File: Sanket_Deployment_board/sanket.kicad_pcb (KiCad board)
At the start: 2 copper layers, 92 x 95.9 mm, 38 parts, among them J1 Conn_01x03, J2 Conn_02x03_Counter_Clockwise, J3 Conn_02x03_Counter_Clockwise, J4 Conn_01x01_Socket, J7 Conn_01x01_Socket, J8 Conn_01x05, Q1 NMOS, Q2 NMOS, U2 SN74LVC1G17QDCKRQ1, U3 TPS5420D, U4 74AHC1G00

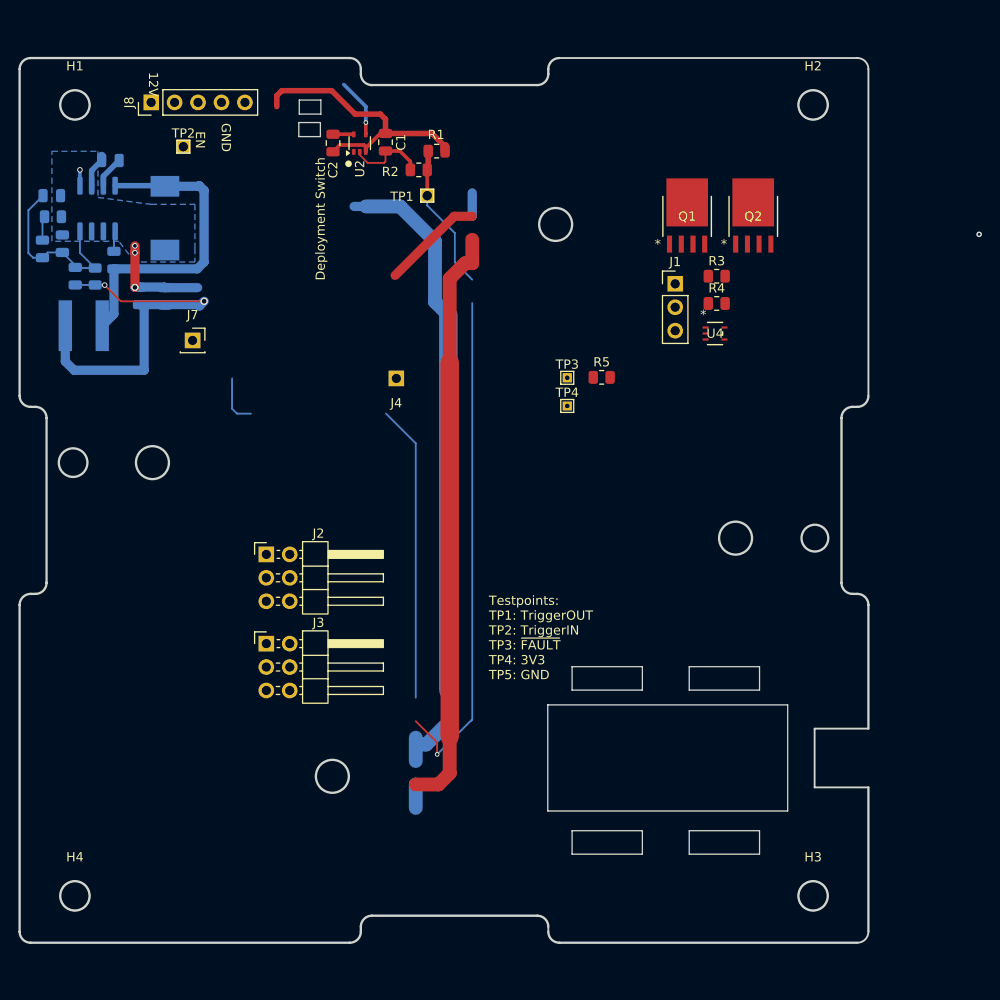
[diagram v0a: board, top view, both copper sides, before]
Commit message: Switch footprint flipped to opposite side, Edgecut layer updated according to new resistor board
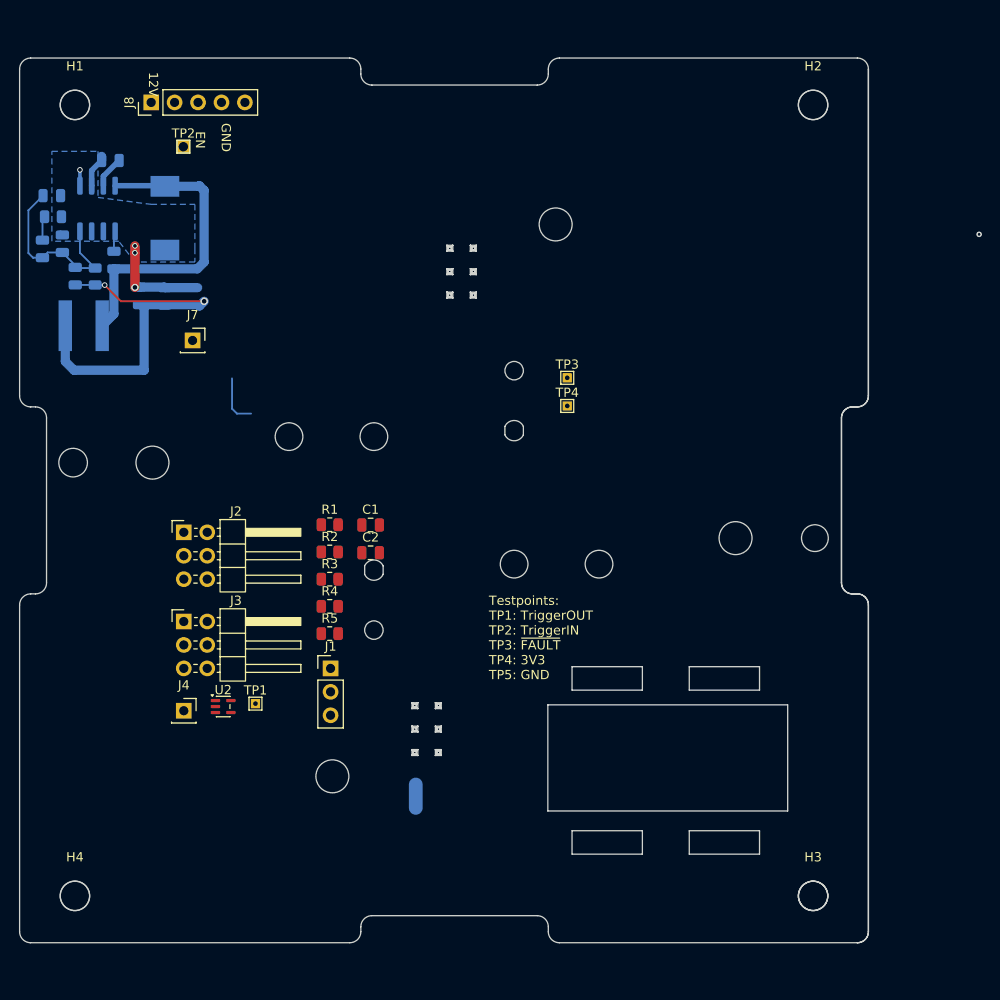
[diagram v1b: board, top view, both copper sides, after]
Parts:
- removed Q1, Q2: NMOS, NMOS_sanket:LFPAK56_SOT669_NEX-M
- removed U4: 74AHC1G00, NAND_sanket:DCK5_TEX-L
- C1: value 2u2 -> ~
- C10: value 4.7u -> ~
- C2, C8: value 100n -> ~
- C3: value 10n -> ~
- C4, C5: value 47u -> ~
- C6: value 150p -> ~
- C9: value 1800p -> ~
- D1: value D -> ~
- H1, H2, H3, H4: value MountingHole -> ~
- J1: value Conn_01x03 -> ~
- J4: value Conn_01x01_Socket -> ~; moved to F.Cu
- J7: value Conn_01x01_Socket -> ~
- J8: value Conn_01x05 -> ~
- L1: value 18u -> ~
- R1: value 1k -> ~
- R2, R3, R4: value 100k -> ~
- R5: value 1M -> ~
- R6: value 549 -> ~
- R7: value 5.9K -> ~
- R8: value 10k -> ~
- TP1, TP2, TP3, TP4: value TestPoint -> ~
- U2: value SN74LVC1G17QDCKRQ1 -> ~
- U3: value TPS5420D -> ~
- moved U2 62.8 mm to (118.4, 119.6), turned to 0 degrees
- moved TP1 58.1 mm to (121.9, 119.3)
- moved J1 56.0 mm to (130.0, 115.4)
- moved R3 53.3 mm to (129.9, 105.8)
- moved R4 53.3 mm to (129.9, 108.7)
- moved C2 44.6 mm to (134.3, 102.9), turned to 0 degrees
- moved J4 42.8 mm to (114.1, 120.0), turned to 0 degrees
- moved R2 42.5 mm to (129.9, 102.8), turned to 0 degrees
- moved R1 42.1 mm to (129.9, 99.9)
- moved C1 41.5 mm to (134.3, 99.9), turned to 0 degrees
- moved R5 40.5 mm to (129.9, 111.7)
- moved J2 9.26 mm to (114.1, 100.7)
- moved J3 9.26 mm to (114.1, 110.4)
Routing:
- net (no net): track 121.1 -> 2.54 mm, vias 2 -> 1
- net /BurnWire1IN: track 70.1 -> 0.00 mm
- net GND: track 60.7 -> 15.9 mm
- net /3V3: track 82.5 -> 48.2 mm
- net /DeployerDetectionSW2OUT: track 16.2 -> 0.00 mm
- net /TriggerIN: track 8.75 -> 0.00 mm
- net /TriggerOUT: track 6.39 -> 0.00 mm, vias 1 -> 0
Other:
- outline, holes or cut-outs redrawn
- board text removed: "Current Sensor"
- board text removed: "Deployment Switch"
- board text removed: "J4"
- board text removed: "TP1"
- board text removed: "TP5"

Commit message: Routing done, 1st review to be done
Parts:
- removed J7: ~, Connector_PinSocket_2.54mm:PinSocket_1x01_P2.54mm_Vertical
- removed TP3, TP4: ~, TestPoint:TestPoint_THTPad_1.0x1.0mm_Drill0.5mm
- added NMOS1: BUK9Y21-40E_115, NMOS_sanket:LFPAK56_SOT669_NEX-M, B.Cu at (116.6, 114.8)
- added NMOS2: BUK9Y21-40E_115, NMOS_sanket:LFPAK56_SOT669_NEX-M, B.Cu at (116.0, 124.1)
- added U1: SN74LV1T00DCKR, NAND_sanket:DCK5_TEX-L, B.Cu at (124.5, 128.3)
- C1, C2, J1, J4, J8, R1, R2, R3, R4, R5, TP1, TP2: moved to B.Cu
- D1: footprint Wurth inductor:DIOM7959X261N -> Diode_in_TP5420:CR_MBRS340_ONS-M
- U2: footprint Package_TO_SOT_SMD:SOT-353_SC-70-5 -> Schmitt_trigger_ADS:DCK5-M; moved to B.Cu
- U3: footprint Package_SO:SOIC-8_3.9x4.9mm_P1.27mm -> TPS5420:D8-M
- moved H4 89.1 mm to (191.3, 143.3), turned to 90 degrees
- moved H1 89.0 mm to (105.6, 143.3), turned to 90 degrees
- moved C6 82.6 mm to (114.7, 145.4), turned to -90 degrees
- moved J8 81.1 mm to (105.3, 135.0), turned to 0 degrees
- moved R6 80.6 mm to (117.0, 145.3), turned to 90 degrees
- moved C8 79.1 mm to (119.8, 146.2), turned to 0 degrees
- moved C10 78.9 mm to (110.2, 139.1), turned to -90 degrees
- moved H3 77.3 mm to (191.3, 63.3), turned to 90 degrees
- moved H2 77.3 mm to (105.6, 63.3), turned to 90 degrees
- moved R7 77.0 mm to (119.8, 144.1), turned to 180 degrees
- moved U3 75.1 mm to (116.0, 139.9), turned to 180 degrees
- moved C9 72.5 mm to (123.4, 142.3), turned to 180 degrees
- moved R8 69.8 mm to (123.4, 140.1), turned to 180 degrees
- moved L1 69.5 mm to (129.8, 142.5), turned to -90 degrees
- moved C3 68.7 mm to (122.5, 138.0), turned to 180 degrees
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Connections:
- J2 pad 1: /3V3 -> /BurnWire1IN
- J2 pad 2: /DeployerDetectionSW1OUT -> /BurnWire1OUT
- J2 pad 4: /BurnWire1IN -> /BurnWire1OUT
- J2 pad 5: /BurnWire1OUT -> /DeployerDetectionSW1OUT
- J2 pad 6: /BurnWire1OUT -> /3V3
- J3 pad 1: /DeployerDetectionSW1OUT -> /BurnWire1OUT
- J3 pad 2: /DeployerDetectionSW2OUT -> /NMOS_DRAIN
- J3 pad 4: /BurnWire1OUT -> /NMOS_DRAIN
- J3 pad 5: GND -> /DeployerDetectionSW2OUT
- J3 pad 6: GND -> /DeployerDetectionSW1OUT
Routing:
- net /BurnWire1IN: track 0.00 -> 85.7 mm
- net /BurnWire1OUT: track 0.00 -> 67.4 mm
- net /3V3: track 48.2 -> 103.5 mm, vias 2 -> 4
- net /DeployerDetectionSW1OUT: track 0.00 -> 46.1 mm
- net /12V: track 3.44 -> 37.6 mm
- net /FIRE: track 0.00 -> 33.5 mm, vias 0 -> 1
- net /DeployerDetectionSW2OUT: track 0.00 -> 20.8 mm
- net /ARM: track 0.00 -> 20.6 mm, vias 0 -> 1
- net Net-(MOSFET1-Pad1): track 0.00 -> 20.1 mm
- net /DEPLOY: track 0.00 -> 19.6 mm
- net /NMOS_DRAIN: track 0.00 -> 18.8 mm
- net /TriggerOUT: track 0.00 -> 7.40 mm
- net /TriggerIN: track 0.00 -> 5.13 mm
- net GND: track 15.9 -> 10.9 mm, vias 3 -> 0
- net Net-(D1-K): track 34.6 -> 30.9 mm, vias 0 -> 2
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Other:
- board size 92 x 95.9 mm -> 95.9 x 92 mm
- board text added: "3V3"
- board text added: "ARM"
- board text added: "BURN1_OUT"
- board text added: "BURNIN"
- board text added: "DEPLOY"
- board text added: "DEPLOYER1_OUT"
- board text added: "FIRE"
- board text removed: "${REFERENCE}"
- board text removed: "Antenna Deployment Board 7 Manyaman Naik, ${COMPANY} 2026-01-09"
- board text removed: "EN"
- board text removed: "TP2"
- board text removed: "TP4"
- board text removed: "Testpoints: TP1: TriggerOUT TP2: TriggerIN TP3: ~{FAULT} TP4: 3V3 TP5: GND"

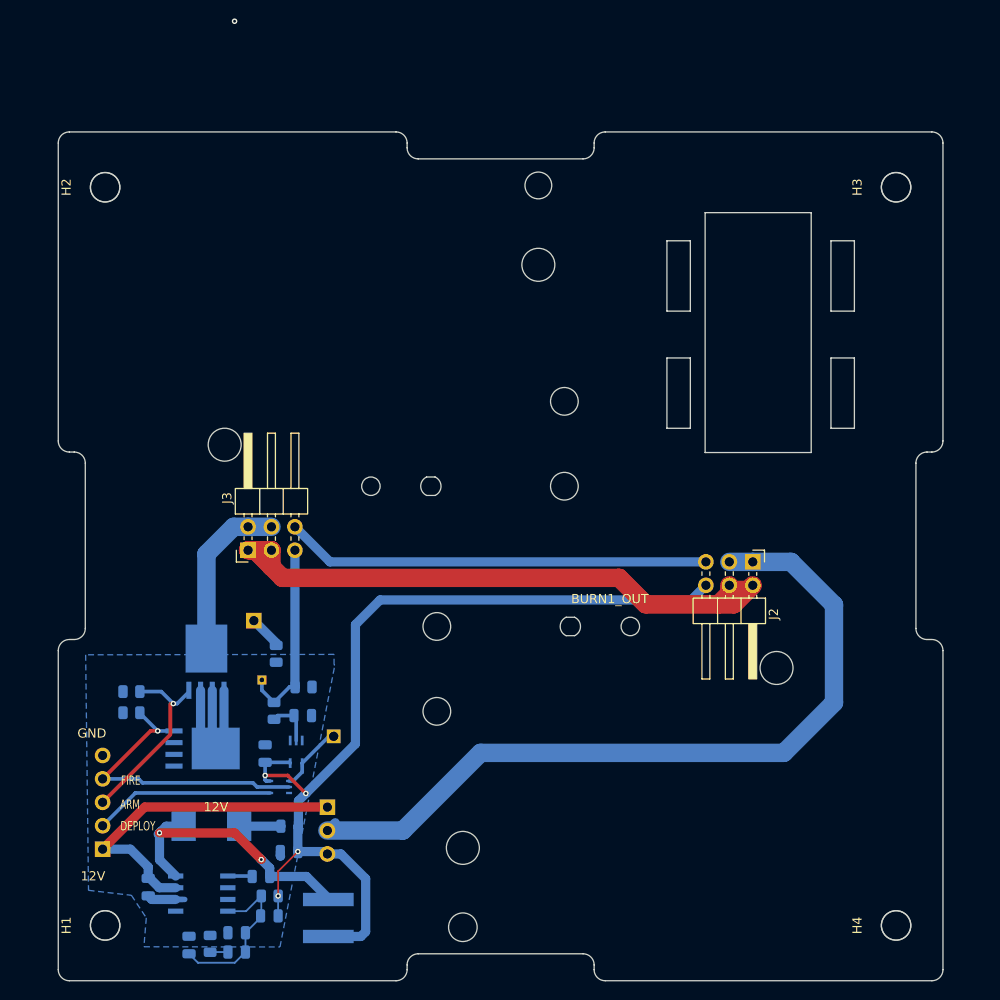
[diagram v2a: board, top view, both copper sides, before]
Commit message: Added missing holw in resistor board, removed NAND gate, added more testpoints
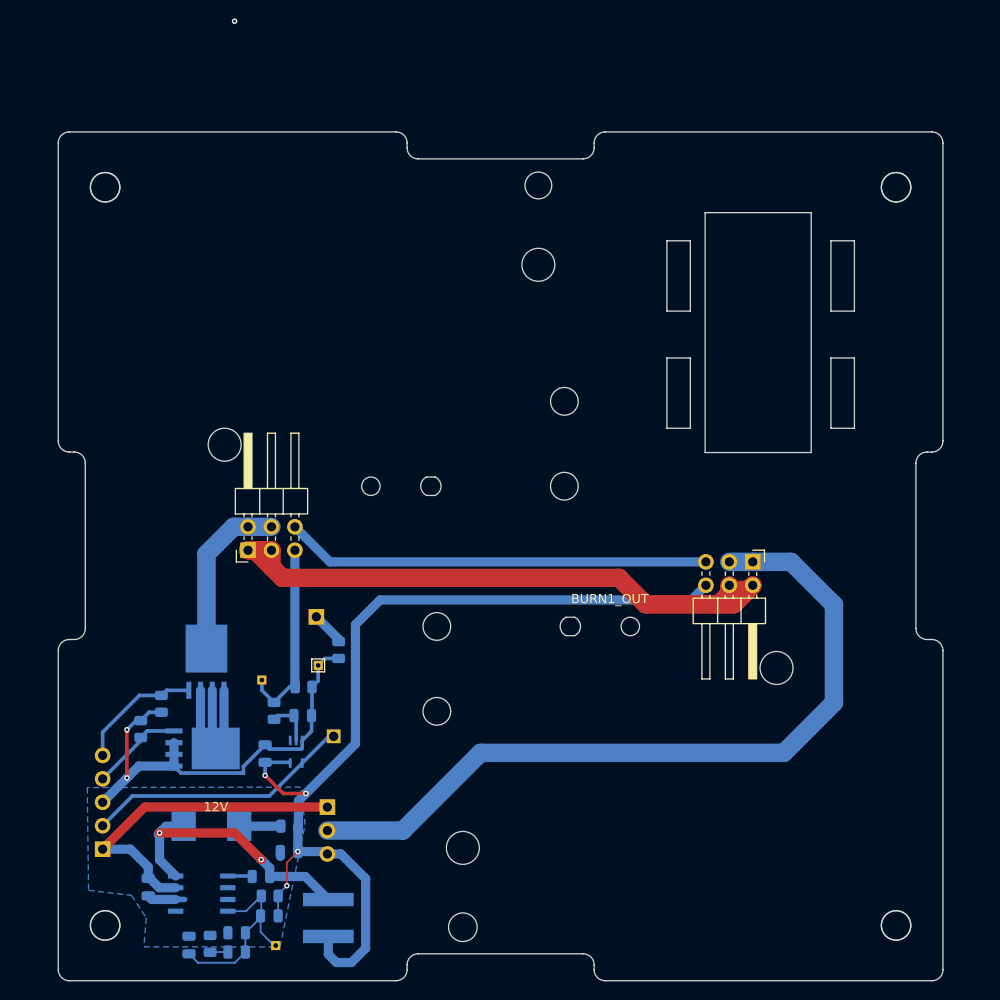
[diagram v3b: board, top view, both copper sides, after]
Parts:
- removed U1: SN74LV1T00DCKR, NAND_sanket:DCK5_TEX-L
- added TP3: ~, TestPoint:TestPoint_THTPad_1.0x1.0mm_Drill0.5mm, B.Cu at (124.1, 145.5)
- added TP4: ~, TestPoint:TestPoint_THTPad_1.0x1.0mm_Drill0.5mm, F.Cu at (128.7, 115.1)
- C1: value ~ -> 2u2
- C10: value ~ -> 4.7u
- C2, C8: value ~ -> 100n
- C4, C5: value ~ -> 47u
- C6: value ~ -> 150p
- L1: value ~ -> 18uH
- R1: value ~ -> 1k
- R2, R3, R4: value ~ -> 100k
- R6: value ~ -> 549
- R7: value ~ -> 5.9k
- R8: value ~ -> 10k
- moved R5 6.78 mm to (130.9, 113.5)
- moved J4 6.78 mm to (128.5, 109.9)
- moved R4 3.51 mm to (111.7, 119.3), turned to 90 degrees
- moved R3 2.04 mm to (109.4, 122.0), turned to -90 degrees
- renumbered NMOS1 to MOSFET1, NMOS2 to MOSFET2
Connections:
- J8 pad 2: /DEPLOY -> /TriggerOUT
- J8 pad 3: /ARM -> GND
- J8 pad 5: GND -> /ARM
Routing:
- net GND: track 10.9 -> 60.8 mm, vias 0 -> 2
- net /FIRE: track 33.5 -> 10.1 mm, vias 1 -> 0
- net /TriggerOUT: track 7.40 -> 29.1 mm
- net /DEPLOY: track 19.6 -> 0.00 mm
- net /ARM: track 20.6 -> 13.9 mm, vias 1 -> 0
- net Net-(U3-VSNS): track 18.7 -> 22.5 mm
- net /3V3: track 103.5 -> 106.9 mm
- net /BurnWire1IN: track 85.7 -> 84.5 mm
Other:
- board text added: "TRIGGER"
- board text removed: "DEPLOY"

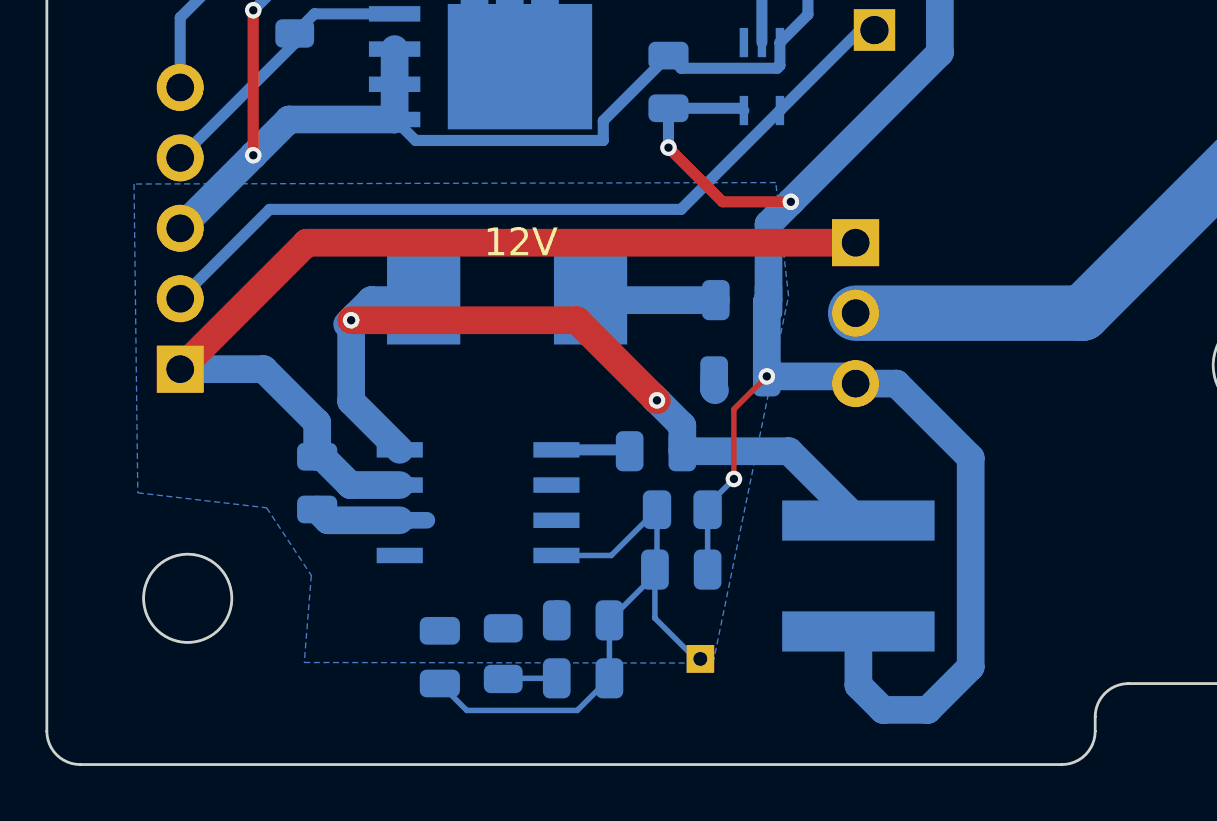
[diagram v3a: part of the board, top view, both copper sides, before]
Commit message: Added extra pads for sized resistors
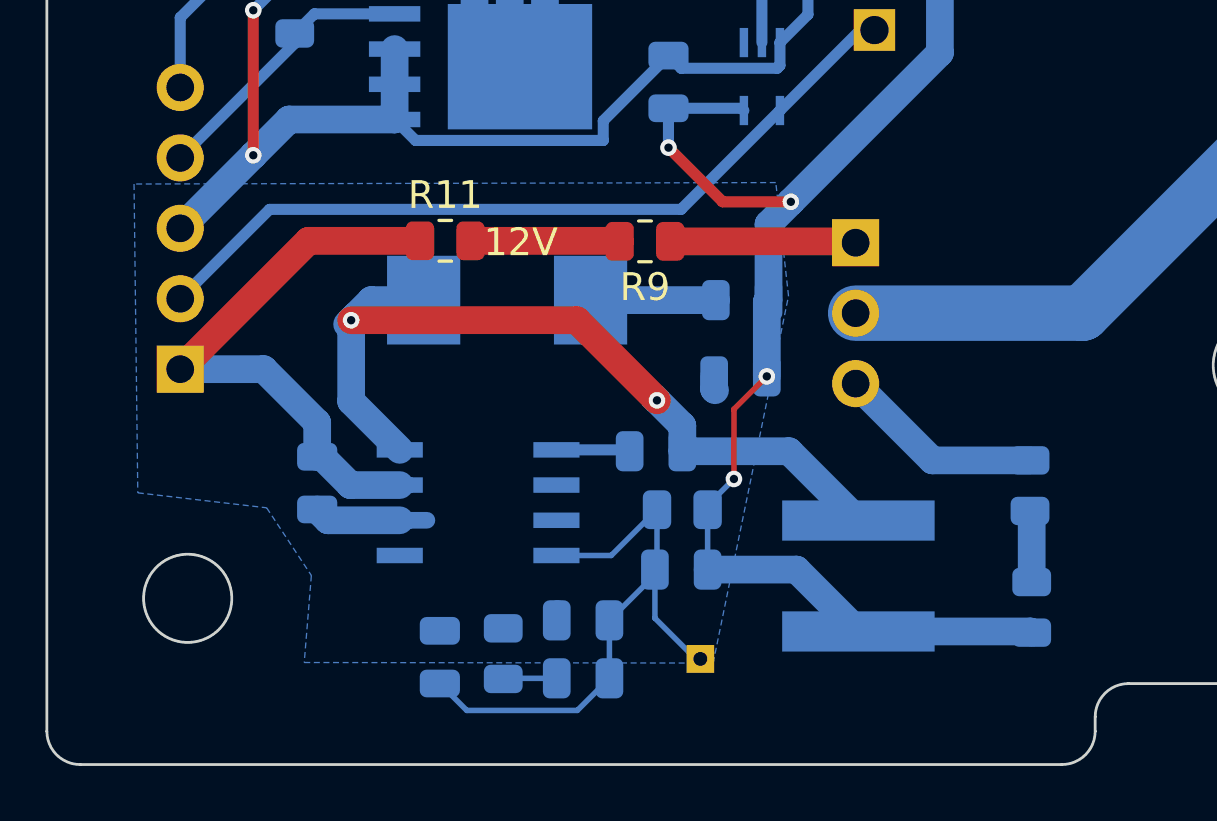
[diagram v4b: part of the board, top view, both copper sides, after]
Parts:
- added R10: R, Resistor_SMD:R_0805_2012Metric, B.Cu at (136.0, 139.2)
- added R11: R, Resistor_SMD:R_0805_2012Metric, F.Cu at (114.9, 130.4)
- added R12: R, Resistor_SMD:R_0805_2012Metric, B.Cu at (136.0, 143.6)
- added R9: R, Resistor_SMD:R_0805_2012Metric, F.Cu at (122.1, 130.4)
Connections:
- J1 pad 1: /12V -> Net-(J1-Pin_1)
- J1 pad 3: /3V3 -> Net-(J1-Pin_3)
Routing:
- net /12V: track 37.6 -> 22.0 mm
- net /3V3: track 106.9 -> 96.4 mm
- net Net-(J1-Pin_3): track 0.00 -> 7.44 mm
- net Net-(J1-Pin_1): track 0.00 -> 6.71 mm
- net Net-(R11-Pad2): track 0.00 -> 5.39 mm
- net Net-(R10-Pad2): track 0.00 -> 2.59 mm

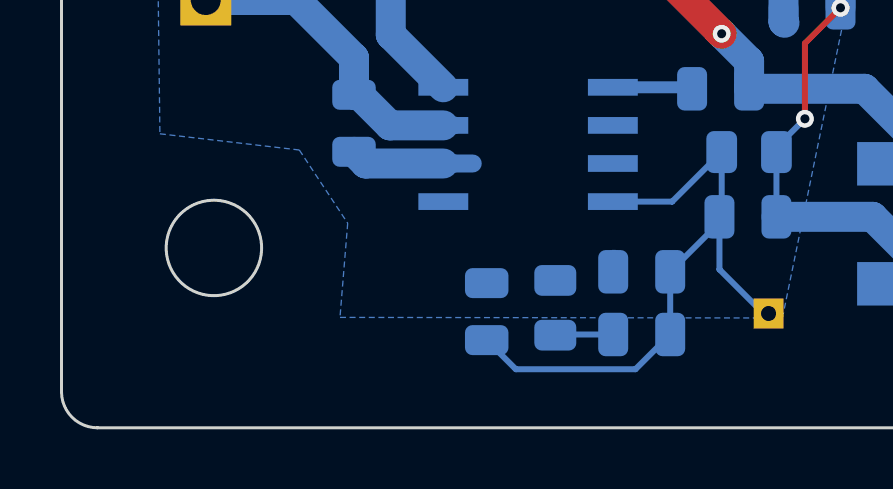
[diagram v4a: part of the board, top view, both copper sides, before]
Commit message: Resistor board for nichrome added
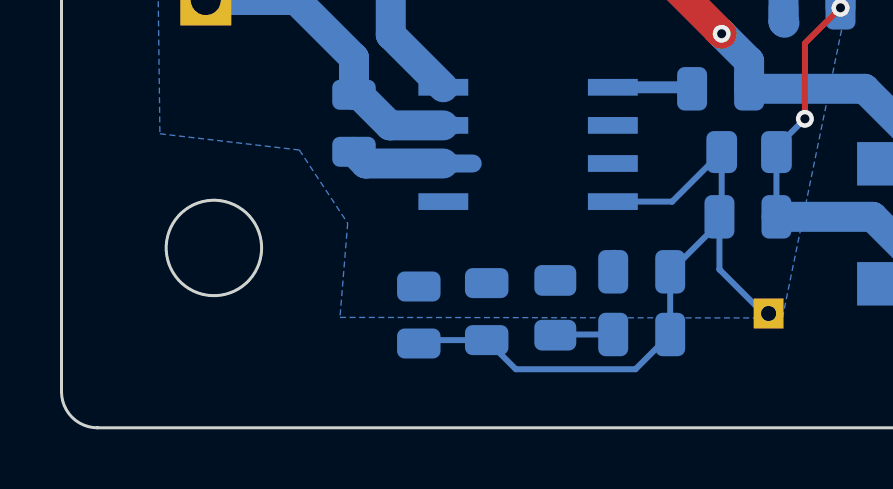
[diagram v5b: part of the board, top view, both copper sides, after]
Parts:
- added C7: 100p, Capacitor_SMD:C_0805_2012Metric, B.Cu at (112.4, 145.5)
- C6: value 150p -> 56p
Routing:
- net Net-(U3-VSNS): track 22.5 -> 24.8 mm
